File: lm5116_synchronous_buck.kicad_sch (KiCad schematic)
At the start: 1 part

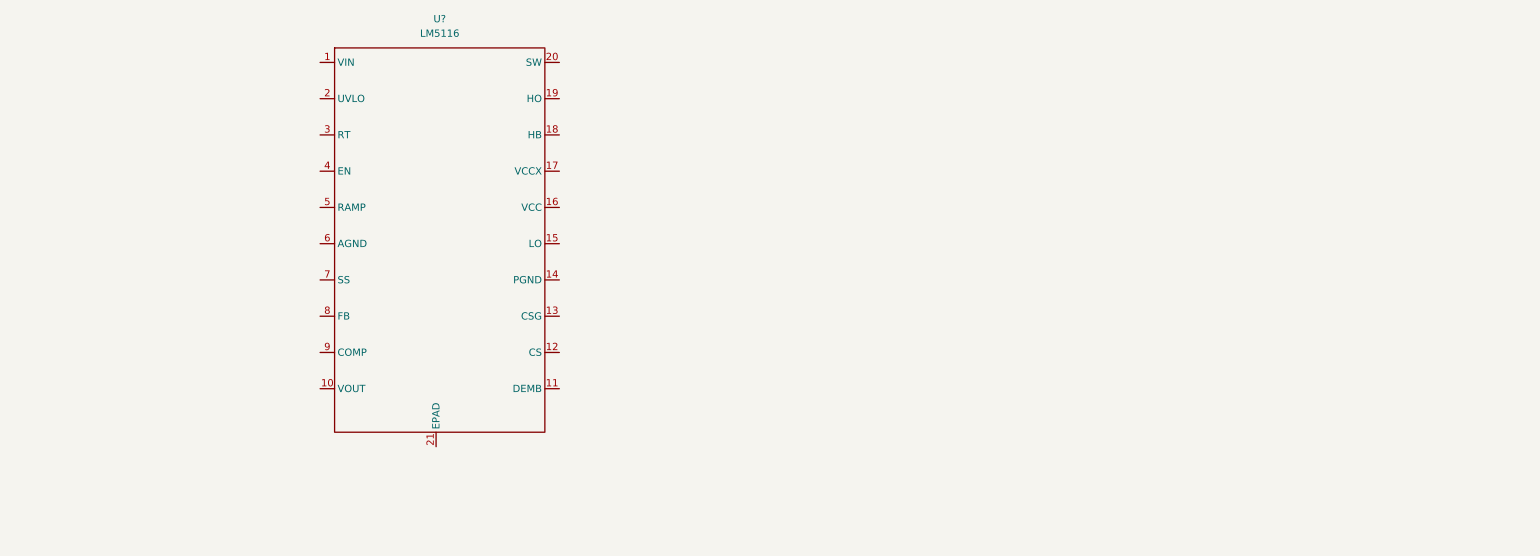
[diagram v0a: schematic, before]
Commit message: * put lm5116 symbol to its own folder
* added stusb4700 symbol
* finished DCDC converter schema
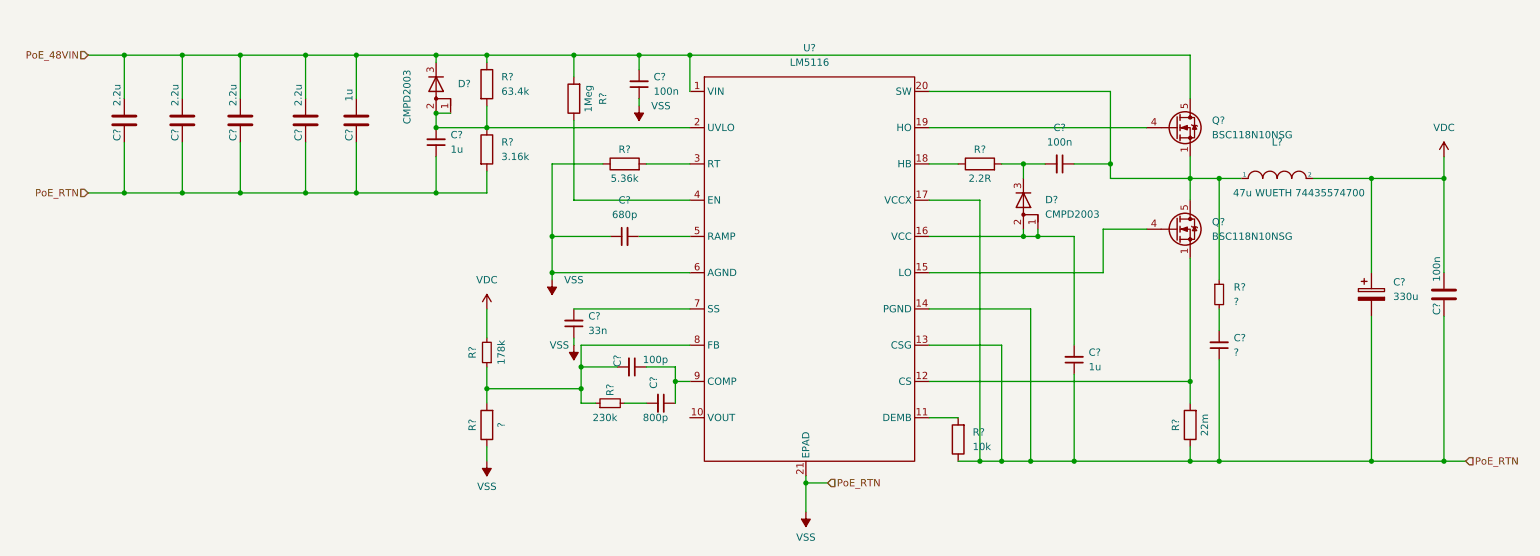
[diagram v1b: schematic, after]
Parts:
- added C?: 800p, symbol Device:C_Small
- added C?: 33n, symbol Device:C_Small
- added C? (x4): 2.2u, symbol Device:C
- added C? (x2): 100n, symbol Device:C_Small
- added C?: 330u, symbol Device:C_Polarized
- added C?: ?, symbol Device:C_Small
- added C?: 100n, symbol Device:C
- added C? (x2): 1u, symbol Device:C_Small
- added C?: 100p, symbol Device:C_Small
- added C?: 1u, symbol Device:C
- added C?: 680p, symbol Device:C_Small
- added D? (x2): CMPD2003, symbol Device:D_AAK
- added L?: 47u WUETH 74435574700, symbol pspice:INDUCTOR
- added Q? (x2): BSC118N10NSG, Package_TO_SOT_SMD:TDSON-8-1, symbol Transistor_FET:BSC118N10NSG
- added R?: 22m, symbol Device:R
- added R?: 1Meg, symbol Device:R
- added R?: ?, symbol Device:R_Small
- added R?: 5.36k, symbol Device:R
- added R?: 3.16k, symbol Device:R
- added R?: 2.2R, symbol Device:R
- added R?: 63.4k, symbol Device:R
- added R?: 178k, symbol Device:R_Small
- added R?: 230k, symbol Device:R_Small
- added R?: 10k, symbol Device:R
- added R?: ?, symbol Device:R
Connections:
- net PoE_48VIN: now reaches U?.1 (VIN)
- net PoE_48VIN: now also C?.1, C?.1, C?.1, C?.1, C?.1, C?.2, D?.3 (K), Q?.5 (D), R?.1, R?.2
- net at U?.11 (DEMB): now also R?.2
- net at U?.12 (CS): now also Q?.1 (S), Q?.2 (S), Q?.3 (S), R?.2
- net VSS: now reaches U?.13 (CSG)
- net VSS: now also U?.14 (PGND), U?.17 (VCCX), U?.21 (EPAD), U?.6 (AGND), C?.1, C?.1, C?.1, C?.1, C?.1, C?.1, C?.2, C?.2, C?.2, C?.2, C?.2, C?.2, C?.2, R?.1, R?.1, R?.1, R?.1, R?.2
- net at U?.15 (LO): now also Q?.4 (G)
- net at U?.16 (VCC): now also C?.2, D?.1 (A), D?.2 (A)
- net at U?.18 (HB): now also R?.1
- net at U?.19 (HO): now also Q?.4 (G)
- net at U?.2 (UVLO): now also C?.2, D?.1 (A), D?.2 (A), R?.1, R?.2
- net at U?.20 (SW): now also C?.1, L?.1, Q?.1 (S), Q?.2 (S), Q?.3 (S), Q?.5 (D), R?.1
- net at U?.3 (RT): now also R?.2
- net at U?.4 (EN): now also R?.1
- net at U?.5 (RAMP): now also C?.2
- net at U?.7 (SS): now also C?.2
- net at U?.8 (FB): now also C?.2, R?.1, R?.1, R?.2
- net at U?.9 (COMP): now also C?.1, C?.1
- new net: C?.2, R?.2 (x2)
- new net: C?.2, D?.3 (K), R?.2
- new net VDC: C?.1, C?.1, L?.2, R?.2
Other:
- moved on the sheet: U?

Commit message: finished schema of lm5116 and USB4700
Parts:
- removed C?: 1u, symbol Device:C
- added C? (x5): 1u, symbol Device:C_Small
- added J? (x5): Conn_01x01_Male, symbol Connector:Conn_01x01_Male
- added Q?: AOD407, symbol Device:Q_PMOS_GDSD
- added Q?: AO3409, symbol Device:Q_PMOS_GDS
- added R?: 3k, symbol Device:R
- added R? (x2): 2k, symbol Device:R
- added R?: 16k, symbol Device:R
- added R?: 1.5k, symbol Device:R
- added R?: 2.2k, symbol Device:R
- added R?: 100k, symbol Device:R
- added R? (x2): 10k, symbol Device:R
- added R?: 4.7k, symbol Device:R
- added R?: 30k, symbol Device:R
- added R?: 2.3k, symbol Device:R
- added U?: STUSB4700, Package_DFN_QFN:QFN-24-1EP_4x4mm_P0.5mm_EP2.7x2.7mm_ThermalVias, symbol STUSB4700:STUSB4700
- R?: value ? -> 11.5k
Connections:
- net PoE_48VIN: now also C?.2, J?.1 (Pin_1)
- net VDC: now also C?.2, J?.1 (Pin_1), Q?.3 (S), R?.2, R?.2, R?.2, U?.24 (VDD)
- net CS: now reaches Q?.1 (S), Q?.2 (S), Q?.3 (S), R?.2, U?.12 (CS)
- net CS: now also J?.1 (Pin_1)
- net SW: now reaches C?.1, L?.1, Q?.1 (S), Q?.2 (S), Q?.3 (S), Q?.5 (D), R?.1, U?.20 (SW)
- net SW: now also J?.1 (Pin_1)
- net FB: now reaches C?.2, R?.1, R?.1, R?.2, U?.8 (FB)
- net VSS renamed GNDPWR
- net GNDPWR: now also C?.1, C?.1, C?.1, C?.1, C?.1, Q?.2 (D), R?.1, R?.1, U?.1 (CC1GND), U?.10 (GND), U?.22 (VSYS), U?.25 (EPAD), U?.3 (VCONN), U?.5 (CC2GND), U?.6 (RESET); no longer R?.1
- new net: R?.1, R?.2, U?.11 (GPIO1)
- new net: R?.1, R?.2, U?.12 (GPIO0)
- new net: R?.2, U?.13 (ADDR0)
- new net: R?.1, R?.2, U?.14 (GPIO2)
- new net: R?.1, R?.2, U?.15 (GPIO3)
- new net: Q?.1 (G), R?.1, U?.19 (VBUS_DISCH)
- new net: R?.1, U?.20 (VBUS_EN_SRC)
- new net: C?.2, U?.21 (VREG_1V2)
- new net: C?.2, U?.23 (VREG_2V7)
- new net: R?.1, R?.2 (x3)
- new net: Q?.1 (G), R?.1, R?.2
- new net: Q?.3 (S), R?.1
- new net SCL: U?.7 (SCL)
- new net SDA: U?.8 (SDA)
- new net USB_CC: U?.2 (CC1)
- new net USB_VBUS: C?.2, J?.1 (Pin_1), Q?.2 (D), Q?.4 (D), U?.18 (VBUS_SENSE)
- new net USB_VCONN: U?.4 (CC2)
- no-connect marks 0 -> 3
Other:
- note added: "LM5116 60W Synchronous Buck Converter"
- note added: "STUSB4700 USBPD Controller"
- note added: "Test Points"
- moved on the sheet: C?, D?, L?, Q?, R?, U?

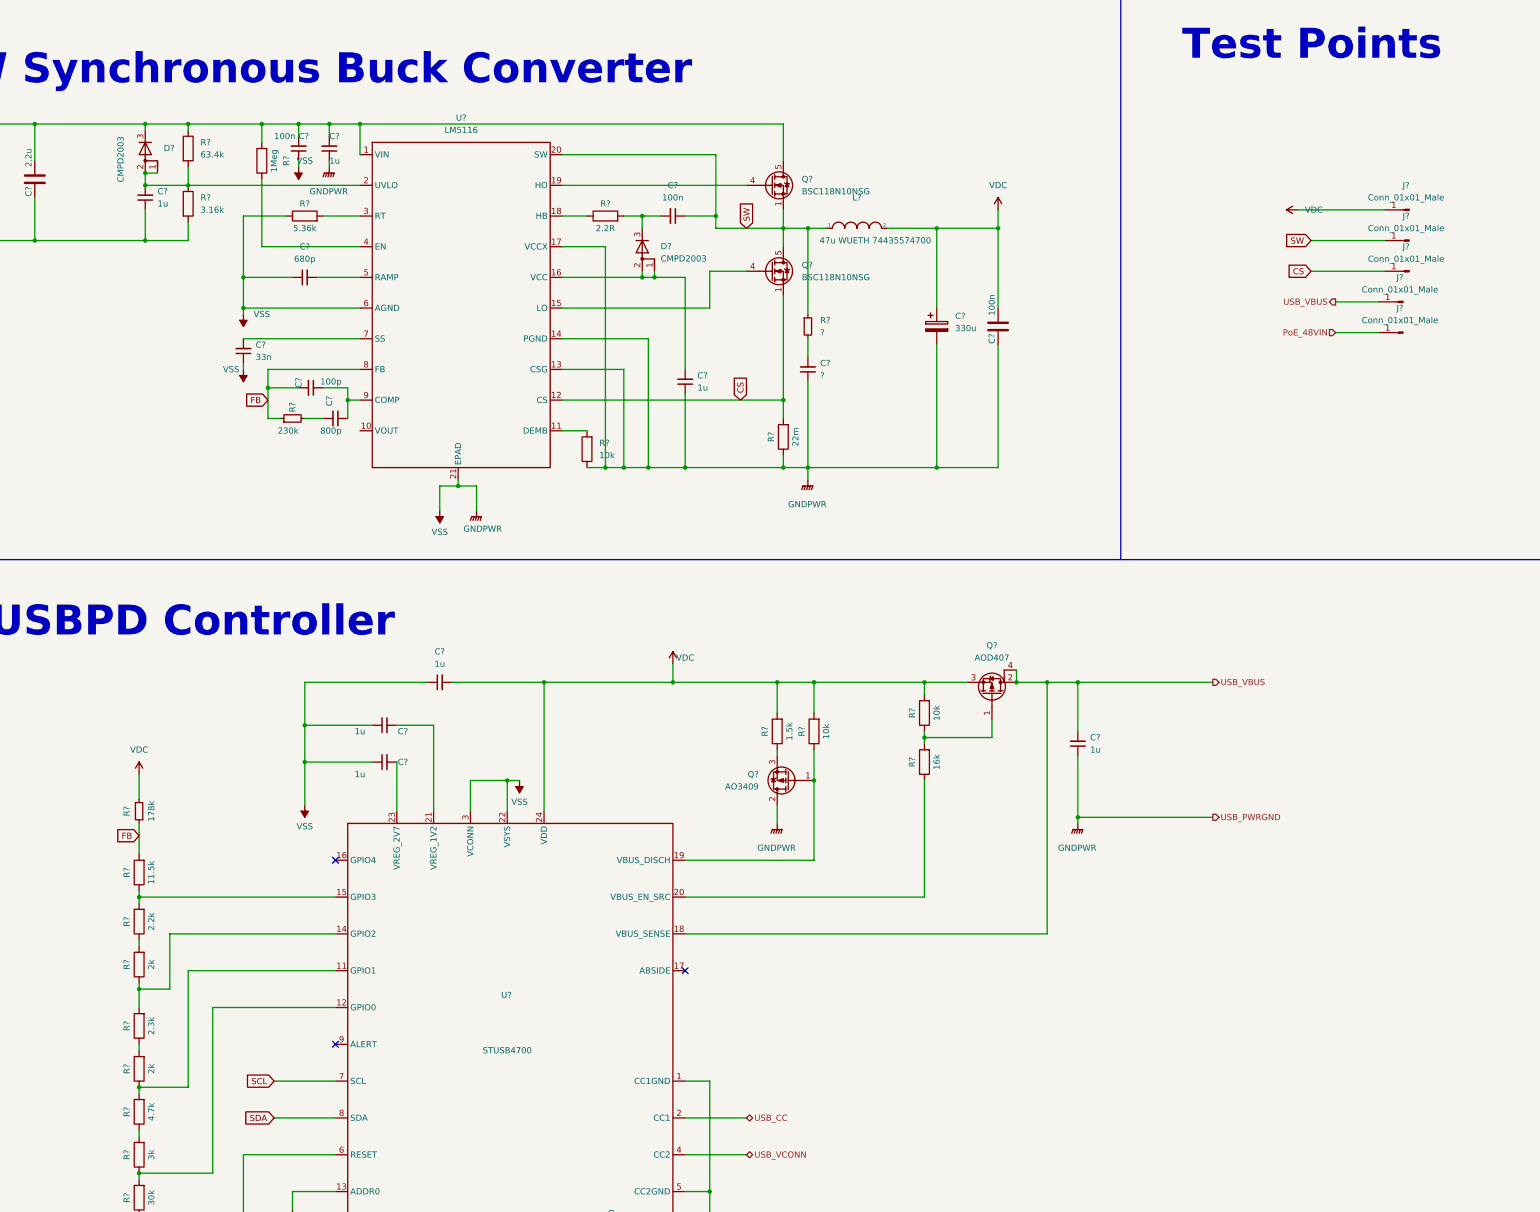
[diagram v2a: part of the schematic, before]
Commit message: added 3v3 for scl & sda pins on stusb4700
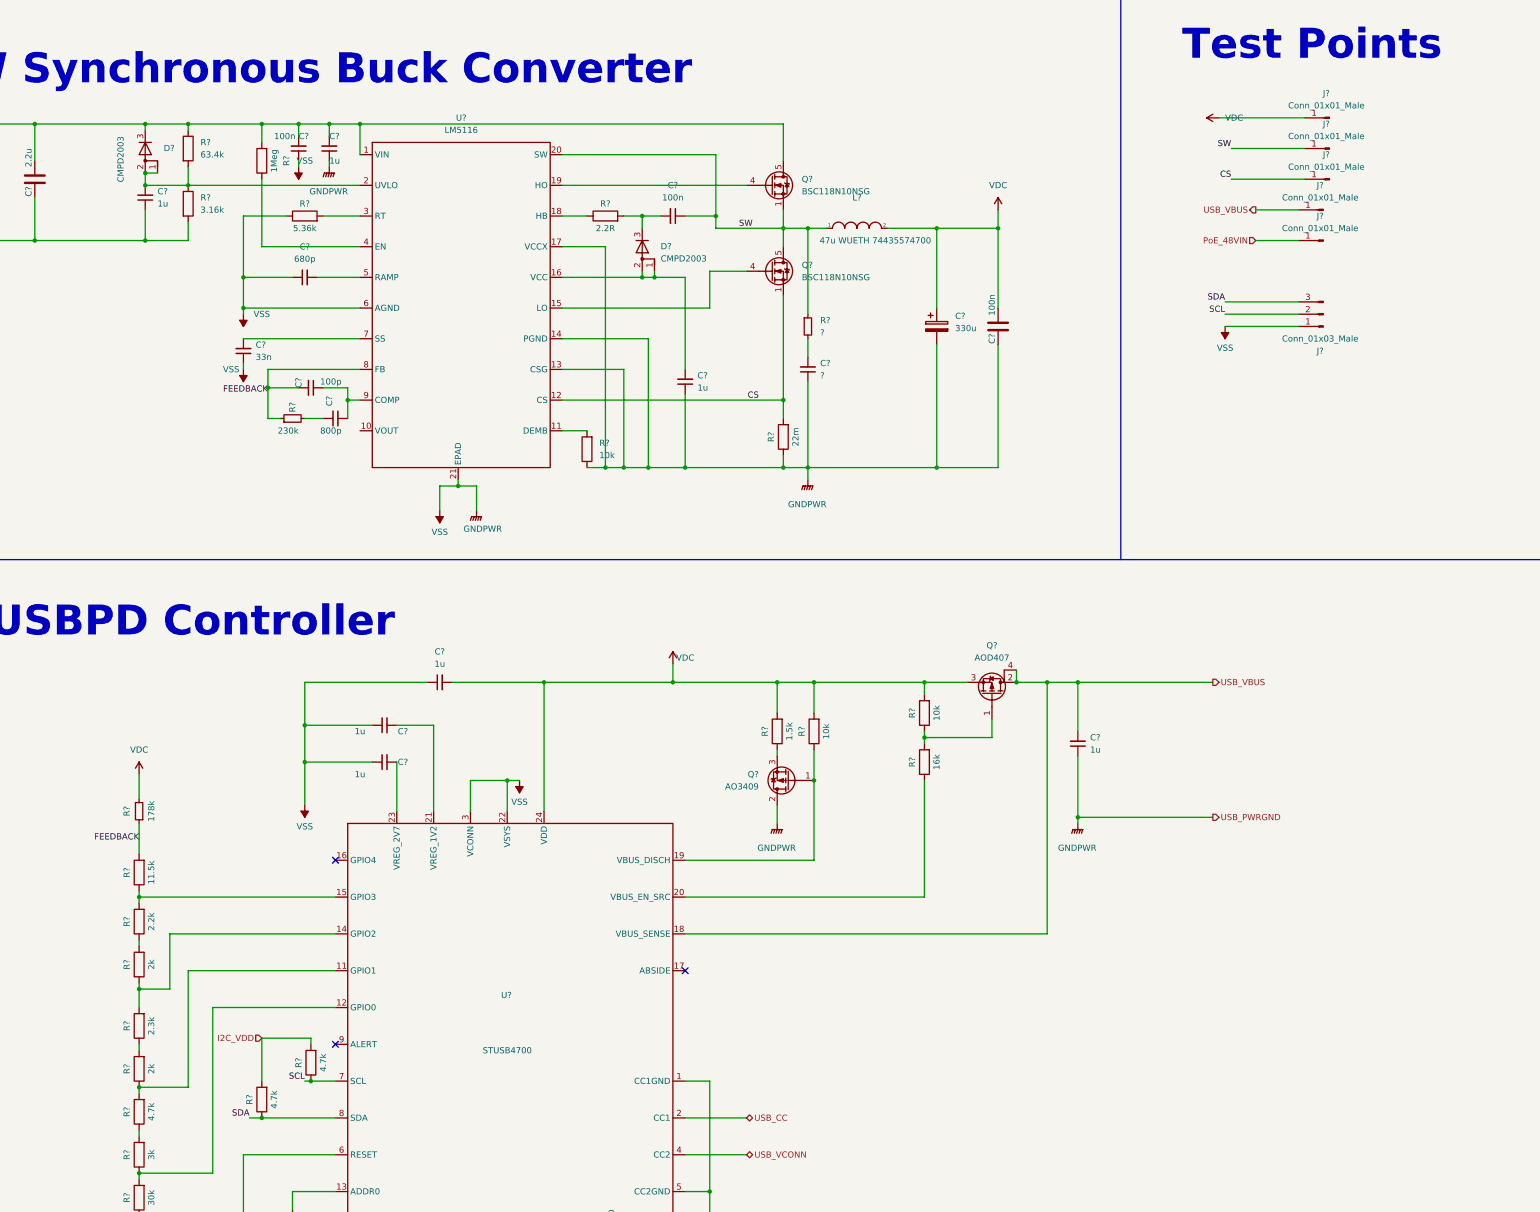
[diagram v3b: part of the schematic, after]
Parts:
- added J?: Conn_01x03_Male, symbol Connector:Conn_01x03_Male
- added R? (x2): 4.7k, symbol Device:R
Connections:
- net GNDPWR: now also J?.1 (Pin_1)
- net SCL: now also J?.2 (Pin_2), R?.1
- net SDA: now also J?.3 (Pin_3), R?.1
- net FB renamed FEEDBACK
- new net I2C_VDD: R?.2, R?.2
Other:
- moved on the sheet: J?
